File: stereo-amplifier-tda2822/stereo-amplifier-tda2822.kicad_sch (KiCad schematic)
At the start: 22 parts, among them J1 PWR IN, J2 AUX IN, J3 SPK 1, J4 SPK 2, U1 TDA2822

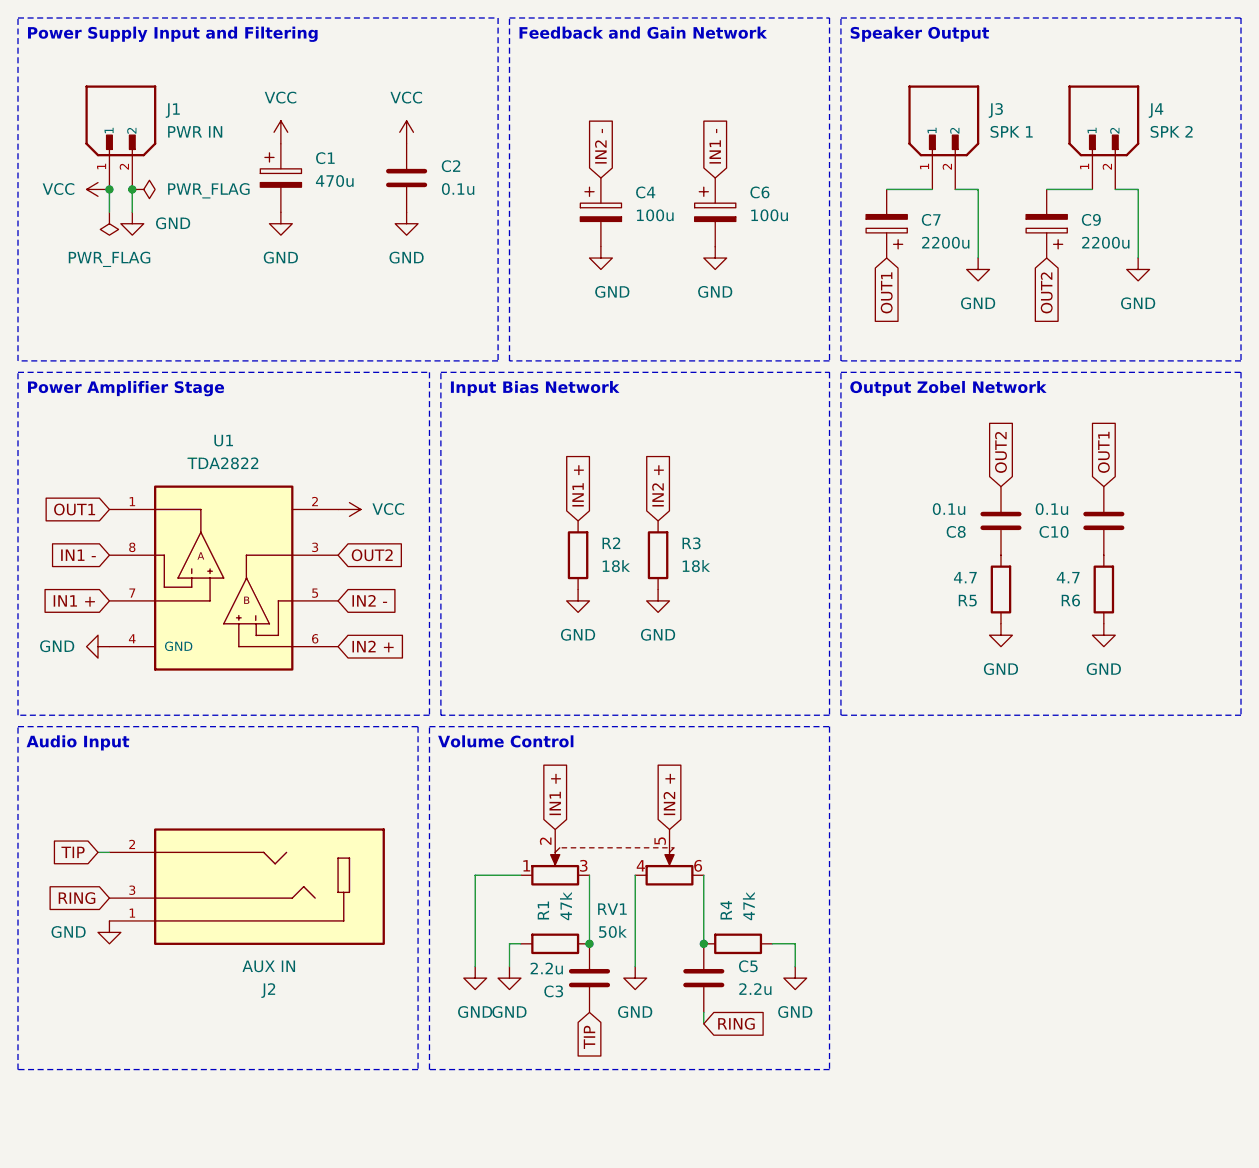
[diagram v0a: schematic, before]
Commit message: Update Stereo Amplifier TDA2822 project
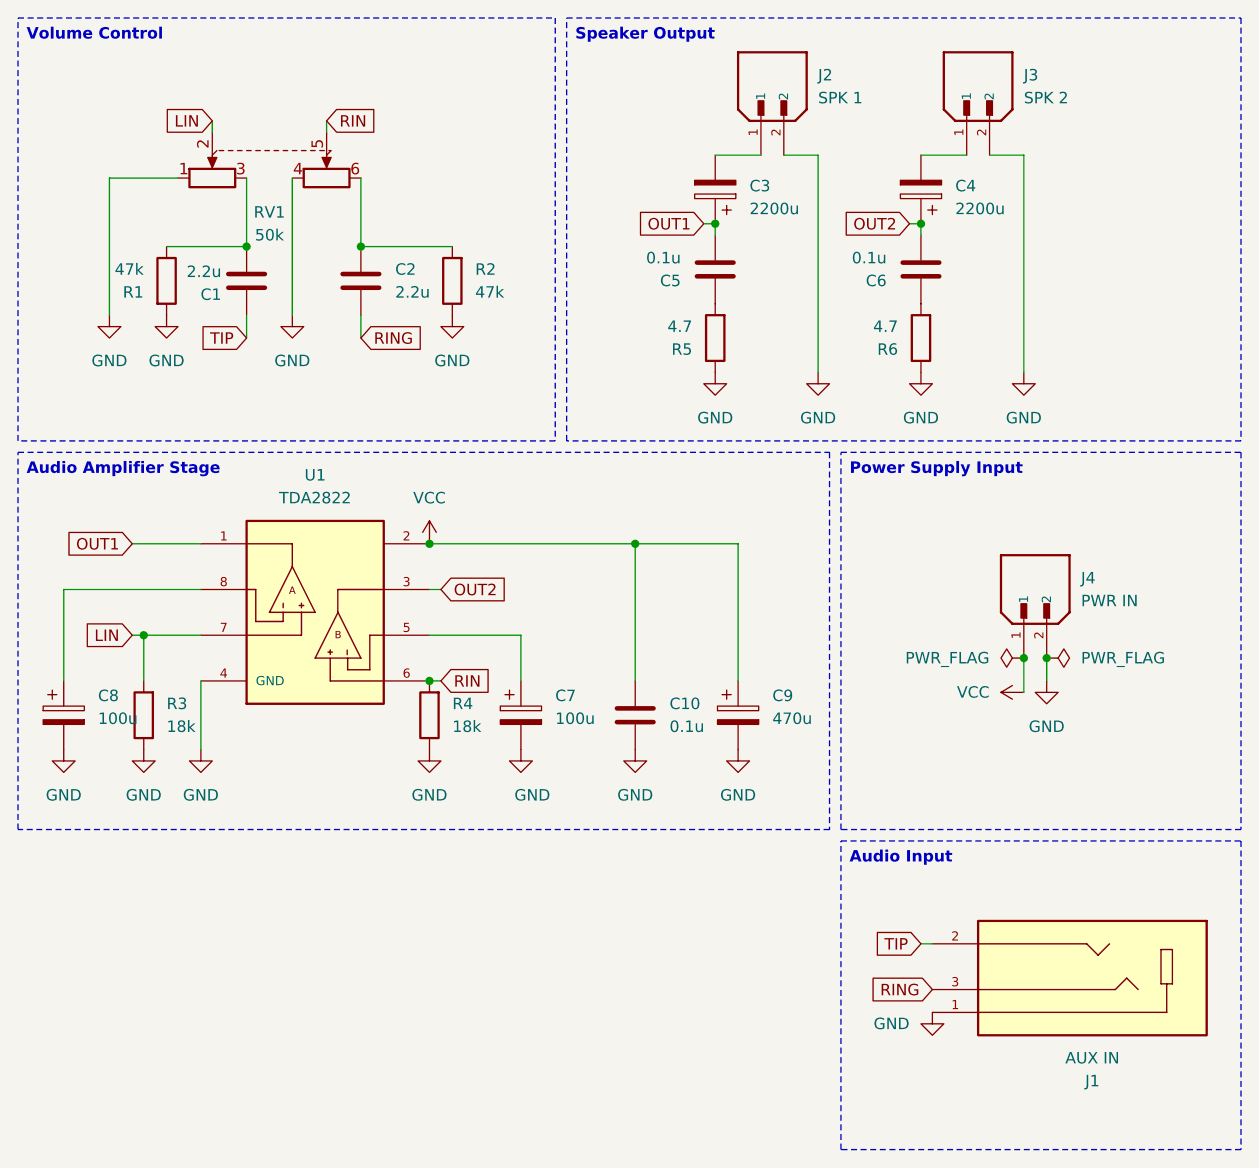
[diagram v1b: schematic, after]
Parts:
- removed C4, C6: 100u, Capacitor_THT:CP_Radial_D5.0mm_P2.50mm, symbol Device:C_Polarized
- removed C8: 0.1u, footprints:CAPRR500W50L730T450H950, symbol Device:C
- added C5: 0.1u, footprints:CAPRR500W50L730T450H950, symbol Device:C
- added C7, C8: 100u, Capacitor_THT:CP_Radial_D5.0mm_P2.50mm, symbol Device:C_Polarized
- renumbered C3 to C1, C2 to C10, C5 to C2, C7 to C3, C9 to C4, C10 to C6, C1 to C9, J2 to J1, J3 to J2, J4 to J3, J1 to J4, R4 to R2, R2 to R3, R3 to R4
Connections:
- net GND: now also C7.2, C8.2
- net OUT1: now also C5.2; no longer C6.2
- net OUT2: now also C6.2
- net at R5.2: now also C5.1
- net IN1 + renamed LIN
- net IN1 -: no longer names the net of U1.8
- net IN1 -: now also C8.1
- net IN2 + renamed RIN
- net IN2 -: no longer names the net of U1.5
- net IN2 -: now also C7.1
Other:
- moved on the sheet: C1, C10, C2, C3, C4, C6, C9, J1, J2, J3, J4, R1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
